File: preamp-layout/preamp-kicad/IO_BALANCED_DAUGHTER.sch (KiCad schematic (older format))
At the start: 59 parts, among them J66 Conn_01x03_Male, J67 Conn_01x03_Male, J68 Conn_01x03_Female, J69 Conn_01x03_Male, J70 XLR3, J71 XLR3, J72 XLR3, J73 XLR3, U20 NJM2068M, U21 NJM2068M, U22 NJM2068M

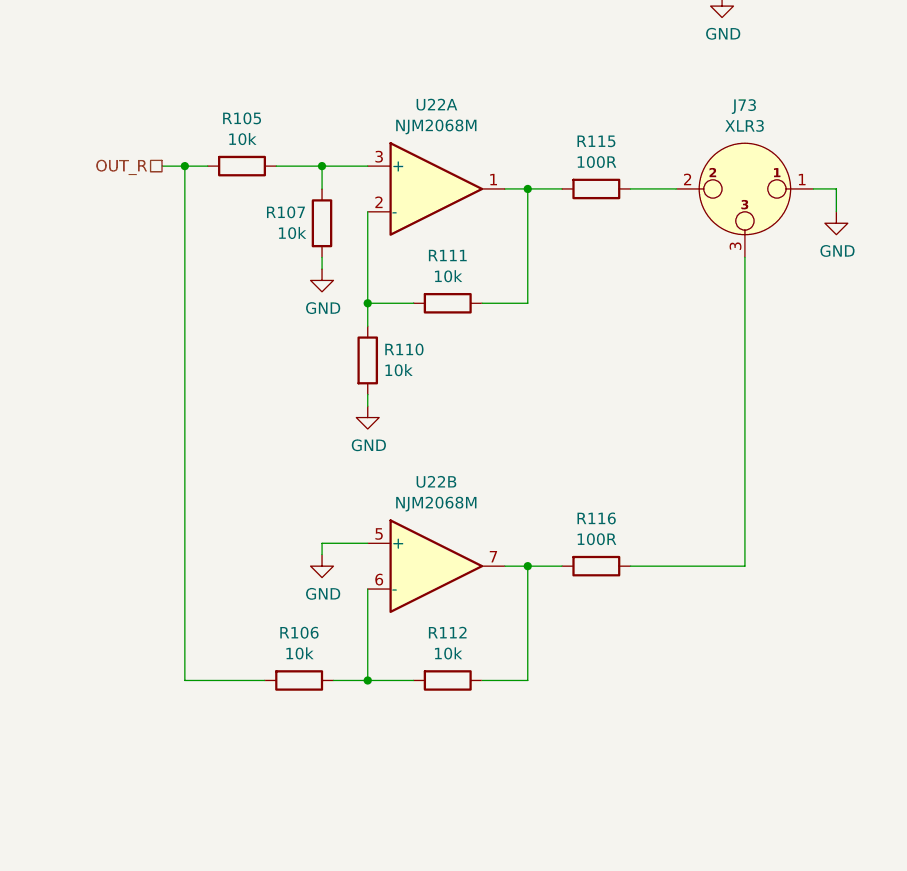
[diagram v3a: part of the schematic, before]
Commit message: Prelim PCB layout
Work done to lay out PCBs. Saving in anticipation of creating branch with a different input switching topology.
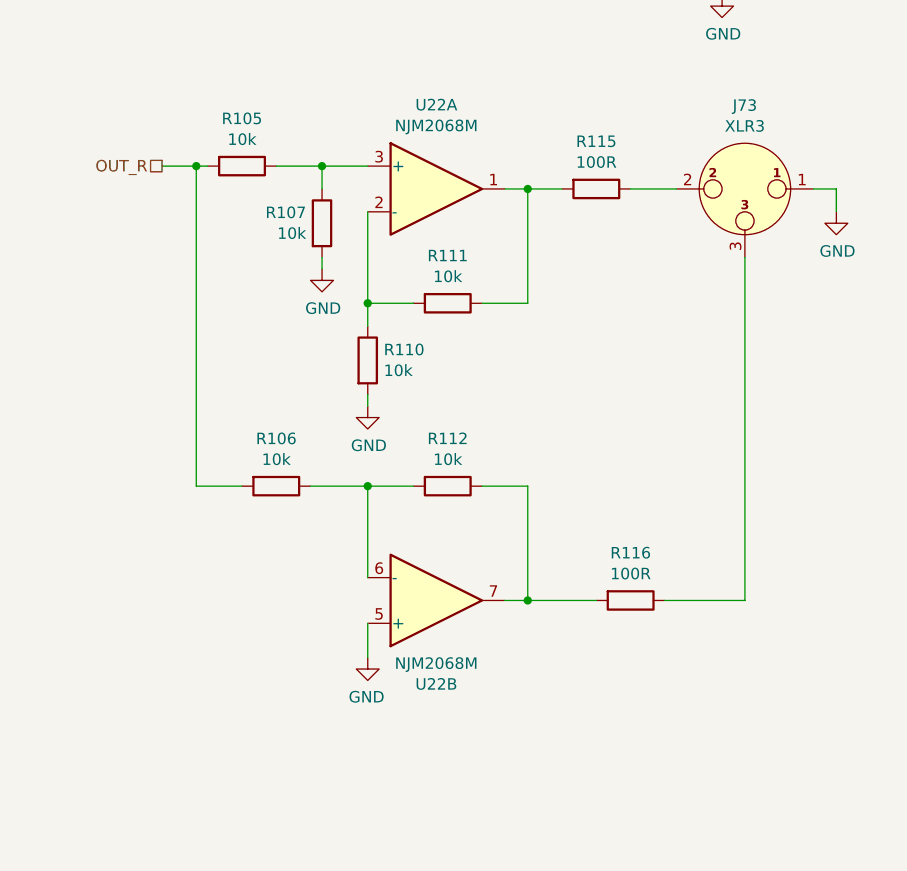
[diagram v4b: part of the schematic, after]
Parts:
- J70, J71, J72, J73: footprint (none) -> Connector_PinHeader_2.54mm:PinHeader_1x03_P2.54mm_Vertical
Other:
- moved on the sheet: R106, R112, R116, U22B
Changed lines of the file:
@@
 L Amplifier_Operational:TL072 U?
 U 2 1 5E1BDF6C
-P 8350 5200
+P 8350 5350
 AR Path="/5E2D8DA2/5E1BDF6C" Ref="U?"  Part="2"
 AR Path="/5E1A0CE1/5E1BDF6C" Ref="U22"  Part="2"
 AR Path="/5E80BFEC/5E1BDF6C" Ref="U?"  Part="2"
-F 0 "U22" H 8350 5567 50  0000 C CNN
-F 1 "NJM2068M" H 8350 5476 50  0000 C CNN
-F 2 "Package_SO:SOP-8_3.9x4.9mm_P1.27mm" H 8350 5200 50  0001 C CNN
-F 3 "http://www.ti.com/lit/ds/symlink/tl071.pdf" H 8350 5200 50  0001 C CNN
-	2    8350 5200
-	1    0    0    -1
-$EndComp
-Wire Wire Line
-	8550 5700 8750 5700
-Wire Wire Line
-	8750 5200 8900 5200
+F 0 "U22" H 8350 5717 50  0000 C CNN
+F 1 "NJM2068M" H 8350 5626 50  0000 C CNN
+F 2 "Package_SO:SOP-8_3.9x4.9mm_P1.27mm" H 8350 5350 50  0001 C CNN
+F 3 "http://www.ti.com/lit/ds/symlink/tl071.pdf" H 8350 5350 50  0001 C CNN
+	2    8350 5350
+	1    0    0    1
+$EndComp
 $Comp
 L Device:R R?
 U 1 1 5E1BDF74
-P 9050 5200
+P 9200 5350
 AR Path="/5E2D8DA2/5E1BDF74" Ref="R?"  Part="1"
 AR Path="/5E1BDF74" Ref="R?"  Part="1"
 AR Path="/5E1A0CE1/5E1BDF74" Ref="R116"  Part="1"
 AR Path="/5E80BFEC/5E1BDF74" Ref="R?"  Part="1"
-F 0 "R116" V 8843 5200 50  0000 C CNN
-F 1 "100R" V 8934 5200 50  0000 C CNN
-F 2 "Resistor_SMD:R_1206_3216Metric_Pad1.42x1.75mm_HandSolder" V 8980 5200 50  0001 C CNN
-F 3 "~" H 9050 5200 50  0001 C CNN
-	1    9050 5200
+F 0 "R116" V 8993 5350 50  0000 C CNN
+F 1 "100R" V 9084 5350 50  0000 C CNN
+F 2 "Resistor_SMD:R_1206_3216Metric_Pad1.42x1.75mm_HandSolder" V 9130 5350 50  0001 C CNN
+F 3 "~" H 9200 5350 50  0001 C CNN
+	1    9200 5350
 	0    1    1    0
 $EndComp
-Connection ~ 8750 5200
-Wire Wire Line
-	8650 5200 8750 5200
-Wire Wire Line
-	8250 5700 8050 5700
-Wire Wire Line
-	7900 5700 8050 5700
-Connection ~ 8050 5700
 $Comp
 L Device:R R?
 U 1 1 5E1BDF85
-P 7750 5700
+P 7650 4850
 AR Path="/5E2D8DA2/5E1BDF85" Ref="R?"  Part="1"
 AR Path="/5E1BDF85" Ref="R?"  Part="1"
 AR Path="/5E1A0CE1/5E1BDF85" Ref="R106"  Part="1"
 AR Path="/5E80BFEC/5E1BDF85" Ref="R?"  Part="1"
-F 0 "R106" V 7543 5700 50  0000 C CNN
-F 1 "10k" V 7634 5700 50  0000 C CNN
-F 2 "Resistor_SMD:R_1206_3216Metric_Pad1.42x1.75mm_HandSolder" V 7680 5700 50  0001 C CNN
-F 3 "~" H 7750 5700 50  0001 C CNN
-	1    7750 5700
+F 0 "R106" V 7443 4850 50  0000 C CNN
+F 1 "10k" V 7534 4850 50  0000 C CNN
+F 2 "Resistor_SMD:R_1206_3216Metric_Pad1.42x1.75mm_HandSolder" V 7580 4850 50  0001 C CNN
+F 3 "~" H 7650 4850 50  0001 C CNN
+	1    7650 4850
 	0    1    1    0
 $EndComp
@@
 L Device:R R?
 U 1 1 5E1BDF8B
-P 8400 5700
+P 8400 4850
 AR Path="/5E2D8DA2/5E1BDF8B" Ref="R?"  Part="1"
 AR Path="/5E1BDF8B" Ref="R?"  Part="1"
 AR Path="/5E1A0CE1/5E1BDF8B" Ref="R112"  Part="1"
 AR Path="/5E80BFEC/5E1BDF8B" Ref="R?"  Part="1"
-F 0 "R112" V 8193 5700 50  0000 C CNN
-F 1 "10k" V 8284 5700 50  0000 C CNN
-F 2 "Resistor_SMD:R_1206_3216Metric_Pad1.42x1.75mm_HandSolder" V 8330 5700 50  0001 C CNN
-F 3 "~" H 8400 5700 50  0001 C CNN
-	1    8400 5700
+F 0 "R112" V 8193 4850 50  0000 C CNN
+F 1 "10k" V 8284 4850 50  0000 C CNN
+F 2 "Resistor_SMD:R_1206_3216Metric_Pad1.42x1.75mm_HandSolder" V 8330 4850 50  0001 C CNN
+F 3 "~" H 8400 4850 50  0001 C CNN
+	1    8400 4850
 	0    1    1    0
 $EndComp
-Wire Wire Line
-	8050 5300 8050 5700
-Wire Wire Line
-	8750 5200 8750 5700
 $Comp
 L Amplifier_Operational:TL072 U?
@@
 F 0 "J70" H 3000 1565 50  0000 C CNN
 F 1 "XLR3" H 3000 1474 50  0000 C CNN
-F 2 "" H 3000 1200 50  0001 C CNN
+F 2 "Connector_PinHeader_2.54mm:PinHeader_1x03_P2.54mm_Vertical" H 3000 1200 50  0001 C CNN
 F 3 " ~" H 3000 1200 50  0001 C CNN
 	1    3000 1200
@@
 F 0 "J72" H 7250 1565 50  0000 C CNN
 F 1 "XLR3" H 7250 1474 50  0000 C CNN
-F 2 "" H 7250 1200 50  0001 C CNN
+F 2 "Connector_PinHeader_2.54mm:PinHeader_1x03_P2.54mm_Vertical" H 7250 1200 50  0001 C CNN
 F 3 " ~" H 7250 1200 50  0001 C CNN
 	1    7250 1200
@@
 F 0 "J71" H 5400 3915 50  0000 C CNN
 F 1 "XLR3" H 5400 3824 50  0000 C CNN
-F 2 "" H 5400 3550 50  0001 C CNN
+F 2 "Connector_PinHeader_2.54mm:PinHeader_1x03_P2.54mm_Vertical" H 5400 3550 50  0001 C CNN
 F 3 " ~" H 5400 3550 50  0001 C CNN
 	1    5400 3550
@@
 F 0 "J73" H 9700 3915 50  0000 C CNN
 F 1 "XLR3" H 9700 3824 50  0000 C CNN
-F 2 "" H 9700 3550 50  0001 C CNN
+F 2 "Connector_PinHeader_2.54mm:PinHeader_1x03_P2.54mm_Vertical" H 9700 3550 50  0001 C CNN
 F 3 " ~" H 9700 3550 50  0001 C CNN
 	1    9700 3550
@@
 Wire Wire Line
 	10000 3550 10100 3550
-Wire Wire Line
-	9700 3850 9700 5200
-Wire Wire Line
-	9200 5200 9700 5200
 Wire Wire Line
 	9200 3550 9400 3550
@@
 Wire Wire Line
 	3000 3450 3100 3450
-Wire Wire Line
-	7150 3450 7250 3450
-Wire Wire Line
-	7250 3450 7250 5700
-Wire Wire Line
-	7250 5700 7600 5700
-Connection ~ 7250 3450
-Wire Wire Line
-	7250 3450 7350 3450
 Wire Wire Line
 	3300 1200 3500 1200
@@
 $EndComp
 $Comp
-L power:GND #PWR?
-U 1 1 5ED698E8
-P 7850 5150
-AR Path="/5E26F6FE/5ED698E8" Ref="#PWR?"  Part="1"
-AR Path="/5E1A0CE1/5ED698E8" Ref="#PWR0118"  Part="1"
-F 0 "#PWR0118" H 7850 4900 50  0001 C CNN
-F 1 "GND" H 7855 4977 50  0000 C CNN
-F 2 "" H 7850 5150 50  0001 C CNN
-F 3 "" H 7850 5150 50  0001 C CNN
-	1    7850 5150
-	1    0    0    -1
-$EndComp
-Wire Wire Line
-	8050 5100 7850 5100
-Wire Wire Line
-	7850 5100 7850 5150
-$Comp
 L Device:C C?
 U 1 1 5F573B27
@@
 	9750 1900 9650 1900
 Connection ~ 9650 1900
+Wire Wire Line
+	7150 3450 7300 3450
+Wire Wire Line
+	8550 4850 8750 4850
+Connection ~ 8750 5350
+Wire Wire Line
+	8650 5350 8750 5350
+Wire Wire Line
+	8250 4850 8050 4850
+Connection ~ 8050 4850
+Wire Wire Line
+	8050 5250 8050 4850
+Wire Wire Line
+	8750 5350 8750 4850
+Wire Wire Line
+	7300 3450 7300 4850
+$Comp
+L power:GND #PWR?
+U 1 1 5EA9883B
+P 8050 5600
+AR Path="/5E26F6FE/5EA9883B" Ref="#PWR?"  Part="1"
+AR Path="/5E1A0CE1/5EA9883B" Ref="#PWR0118"  Part="1"
+F 0 "#PWR0118" H 8050 5350 50  0001 C CNN
+F 1 "GND" H 8055 5427 50  0000 C CNN
+F 2 "" H 8050 5600 50  0001 C CNN
+F 3 "" H 8050 5600 50  0001 C CNN
+	1    8050 5600
+	-1   0    0    -1
+$EndComp
+Wire Wire Line
+	9700 3850 9700 5350
+Wire Wire Line
+	7800 4850 8050 4850
+Wire Wire Line
+	7500 4850 7300 4850
+Wire Wire Line
+	8750 5350 9050 5350
+Wire Wire Line
+	9350 5350 9700 5350
+Wire Wire Line
+	8050 5450 8050 5600
+Connection ~ 7300 3450
+Wire Wire Line
+	7300 3450 7350 3450
 $EndSCHEMATC

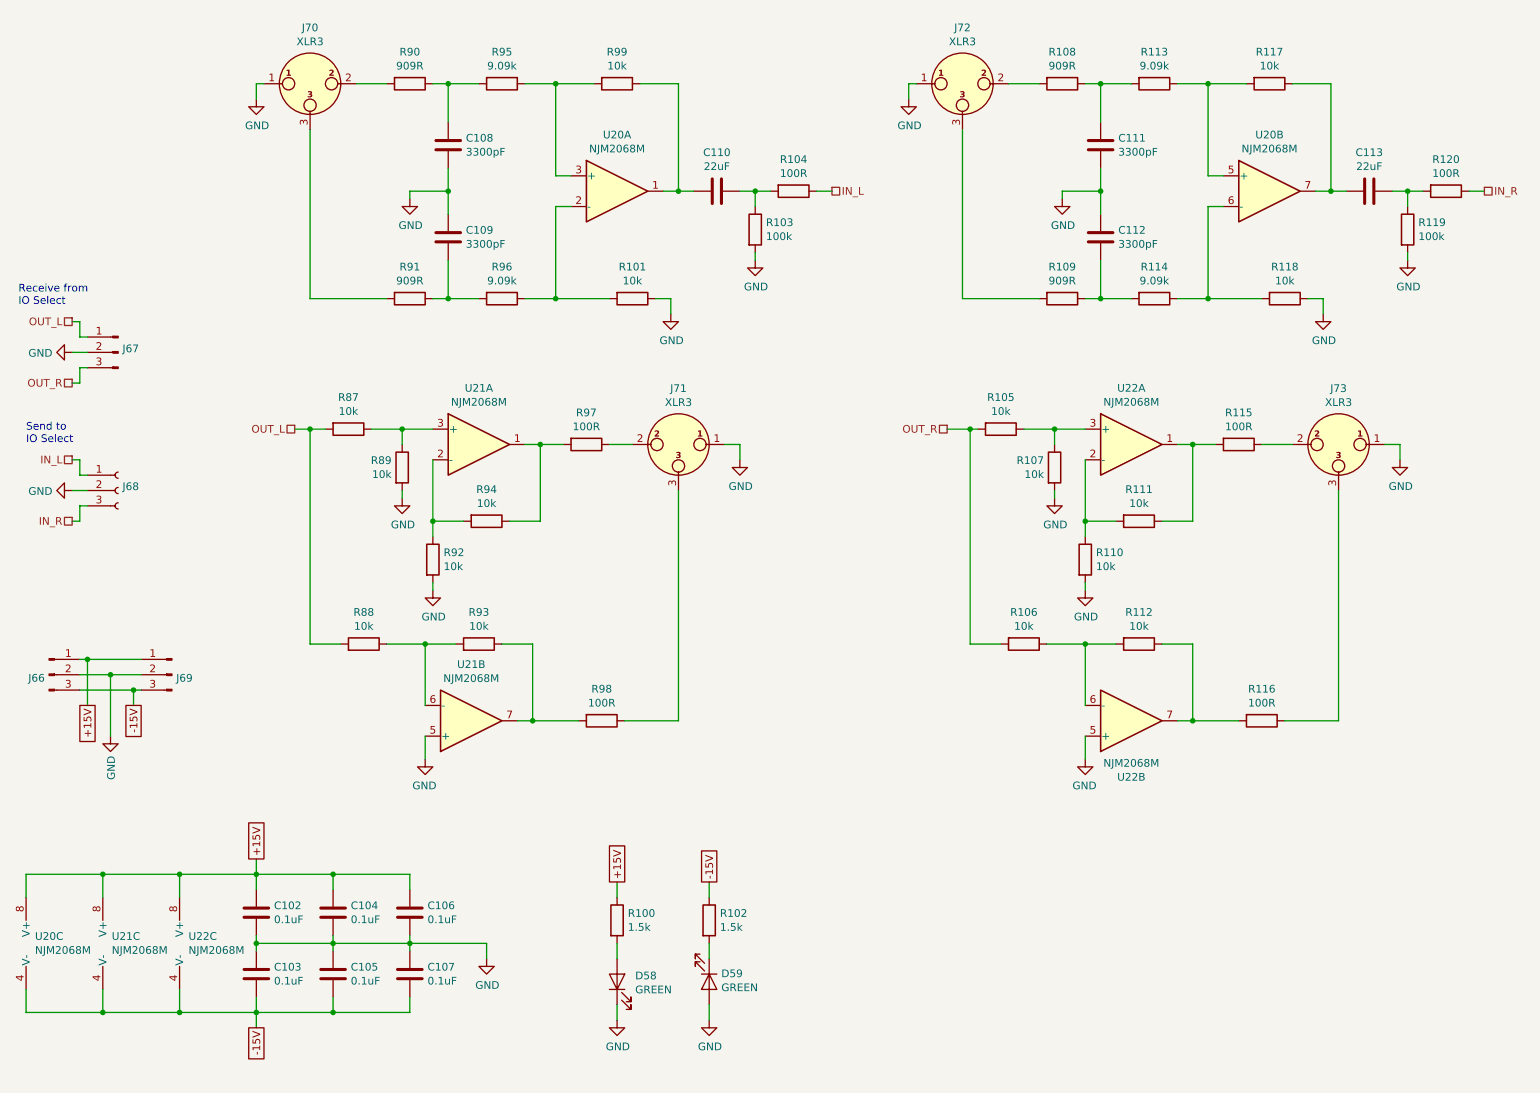
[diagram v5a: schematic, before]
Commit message: Balanced in/out update
Created THAT1646, THAT1280 schematic symbols an implemented in the balanced IO daughter card. Various layout updates as well, this is WIP.
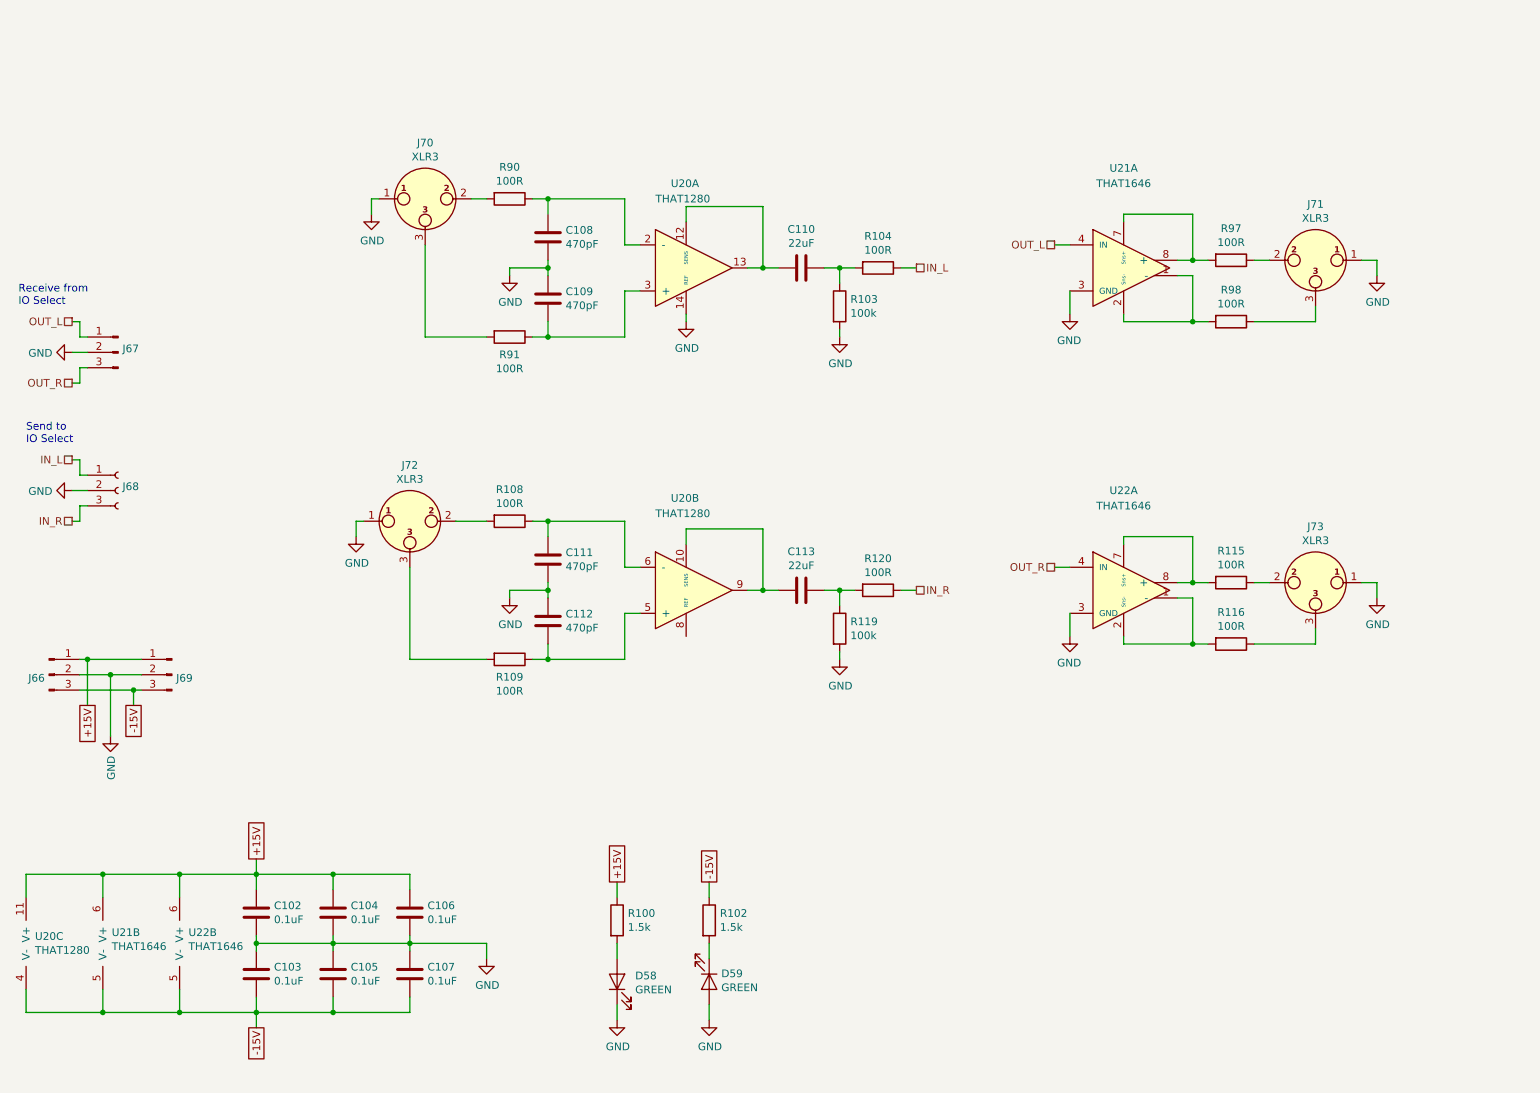
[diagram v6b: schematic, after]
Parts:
- removed R101, R105, R106, R107, R110, R111, R112, R117, R118, R87, R88, R89, R92, R93, R94, R99: 10k, Resistor_SMD:R_1206_3216Metric_Pad1.42x1.75mm_HandSolder, symbol Device:R
- removed R113, R114, R95, R96: 9.09k, Resistor_SMD:R_1206_3216Metric_Pad1.42x1.75mm_HandSolder, symbol Device:R
- removed U20, U21, U22: NJM2068M, Package_SO:SOP-8_3.9x4.9mm_P1.27mm, symbol Amplifier_Operational:TL072
- added U20: THAT1280, symbol preamp:THAT1280
- added U21, U22: THAT1646, symbol preamp:THAT1646
- C108, C109, C111, C112: value 3300pF -> 470pF
- R108, R109, R90, R91: value 909R -> 100R
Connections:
- net +15V: now also U20.11 (V+), U21.6 (V+), U22.6 (V+)
- net -15V: now also U20.4 (V-), U21.5 (V-), U22.5 (V-)
- net GND: now also U20.14 (REF), U21.3 (GND), U22.3 (GND)
- net OUT_L: now also U21.4 (IN)
- net OUT_R: now also U22.4 (IN)
- net at C110.1: now also U20.12 (SENS), U20.13
- net at C109.2, R91.1: now also U20.3 (+)
- net at C108.1, R90.1: now also U20.2 (-)
- net at C113.1: now also U20.10 (SENS), U20.9
- net at C112.2, R109.1: now also U20.5 (+)
- net at C111.1, R108.1: now also U20.6 (-)
- net at R98.2: now also U21.1 (-), U21.2 (Sns-)
- net at R97.2: now also U21.7 (Sns+), U21.8 (+)
- net at R115.2: now also U22.7 (Sns+), U22.8 (+)
- net at R116.2: now also U22.1 (-), U22.2 (Sns-)
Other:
- moved on the sheet: C108, C109, C110, C111, C112, C113, J70, J71, J72, J73, R103, R104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

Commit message: PCB layout
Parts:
- removed J66, J69: Conn_01x03_Male, Connector_JST:JST_EH_B3B-EH-A_1x03_P2.50mm_Vertical, symbol Connector:Conn_01x03_Male
- removed J67: Conn_01x03_Male, Connector_PinHeader_2.54mm:PinHeader_1x03_P2.54mm_Vertical, symbol Connector:Conn_01x03_Male
- removed J68: Conn_01x03_Female, Connector_PinHeader_2.54mm:PinHeader_1x03_P2.54mm_Vertical, symbol Connector:Conn_01x03_Female
- added J50, J53: Conn_01x04_Male, Connector_JST:JST_EH_B4B-EH-A_1x04_P2.50mm_Vertical, symbol Connector:Conn_01x04_Male
- added J67: Conn_01x05_Male, Connector_PinHeader_2.54mm:PinHeader_1x05_P2.54mm_Vertical, symbol Connector:Conn_01x05_Male
- U20: footprint (none) -> Package_SO:SOIC-14_3.9x8.7mm_P1.27mm
- U21, U22: footprint (none) -> Package_SO:SOIC-8_3.9x4.9mm_P1.27mm
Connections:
- net +15V: now also J50.1 (Pin_1), J53.1 (Pin_1)
- net -15V: now also J50.2 (Pin_2), J53.2 (Pin_2)
- net GND: now also U20.8 (REF), J50.3 (Pin_3), J53.3 (Pin_3), J67.3 (Pin_3)
- net IN_L: now also J67.4 (Pin_4)
- net IN_R: now also J67.5 (Pin_5)
- net OUT_L: now also J67.1 (Pin_1)
- net OUT_R: now also J67.2 (Pin_2)
- new net +5V: J50.4 (Pin_4), J53.4 (Pin_4)
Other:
- note removed: "Receive from\nIO Select"
- note removed: "Send to\nIO Select"

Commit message: PCB layout update, front panel and LED restructure
Restructure of capacitive buttons. Restructure of MCU schematic. Moved LEDs to front panel sheet. Front panel and MCU initial PCB layout. 8 bit DAC update (grounded address pins). DAC connection renaming. Added mounting holes for boards.
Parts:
- added H29, H30, H31, H32: MountingHole, MountingHole:MountingHole_3.2mm_M3, symbol Mechanical:MountingHole
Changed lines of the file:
@@
 Wire Wire Line
 	2050 4950 2300 4950
+$Comp
+L Mechanical:MountingHole H?
+U 1 1 5EE3C695
+P 6750 6850
+AR Path="/5EE3C695" Ref="H?"  Part="1"
+AR Path="/5E2D8DA2/5EE3C695" Ref="H?"  Part="1"
+AR Path="/5E1A0CE1/5EE3C695" Ref="H29"  Part="1"
+F 0 "H29" H 6850 6850 50  0001 L CNN
+F 1 "MountingHole" H 6850 6805 50  0001 L CNN
+F 2 "MountingHole:MountingHole_3.2mm_M3" H 6750 6850 50  0001 C CNN
+F 3 "~" H 6750 6850 50  0001 C CNN
+	1    6750 6850
+	1    0    0    -1
+$EndComp
+$Comp
+L Mechanical:MountingHole H?
+U 1 1 5EE3C69B
+P 6750 7050
+AR Path="/5EE3C69B" Ref="H?"  Part="1"
+AR Path="/5E2D8DA2/5EE3C69B" Ref="H?"  Part="1"
+AR Path="/5E1A0CE1/5EE3C69B" Ref="H30"  Part="1"
+F 0 "H30" H 6850 7050 50  0001 L CNN
+F 1 "MountingHole" H 6850 7005 50  0001 L CNN
+F 2 "MountingHole:MountingHole_3.2mm_M3" H 6750 7050 50  0001 C CNN
+F 3 "~" H 6750 7050 50  0001 C CNN
+	1    6750 7050
+	1    0    0    -1
+$EndComp
+$Comp
+L Mechanical:MountingHole H?
+U 1 1 5EE3C6A1
+P 6750 7250
+AR Path="/5EE3C6A1" Ref="H?"  Part="1"
+AR Path="/5E2D8DA2/5EE3C6A1" Ref="H?"  Part="1"
+AR Path="/5E1A0CE1/5EE3C6A1" Ref="H31"  Part="1"
+F 0 "H31" H 6850 7250 50  0001 L CNN
+F 1 "MountingHole" H 6850 7205 50  0001 L CNN
+F 2 "MountingHole:MountingHole_3.2mm_M3" H 6750 7250 50  0001 C CNN
+F 3 "~" H 6750 7250 50  0001 C CNN
+	1    6750 7250
+	1    0    0    -1
+$EndComp
+$Comp
+L Mechanical:MountingHole H?
+U 1 1 5EE3C6A7
+P 6750 7450
+AR Path="/5EE3C6A7" Ref="H?"  Part="1"
+AR Path="/5E2D8DA2/5EE3C6A7" Ref="H?"  Part="1"
+AR Path="/5E1A0CE1/5EE3C6A7" Ref="H32"  Part="1"
+F 0 "H32" H 6850 7450 50  0001 L CNN
+F 1 "MountingHole" H 6850 7405 50  0001 L CNN
+F 2 "MountingHole:MountingHole_3.2mm_M3" H 6750 7450 50  0001 C CNN
+F 3 "~" H 6750 7450 50  0001 C CNN
+	1    6750 7450
+	1    0    0    -1
+$EndComp
 $EndSCHEMATC
